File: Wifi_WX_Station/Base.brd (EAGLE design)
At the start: 91.4 x 50.8 mm, 75 parts, among them IC1 3.3v, J1 RJ45-8VERT, J5 RJ11-6RJ11-VERT_LP, J6 M05X22X5FE, Q1 32.768Khz, U1 CP2104-GM, U2 25LC512, U3 PIC24FJ128GA008

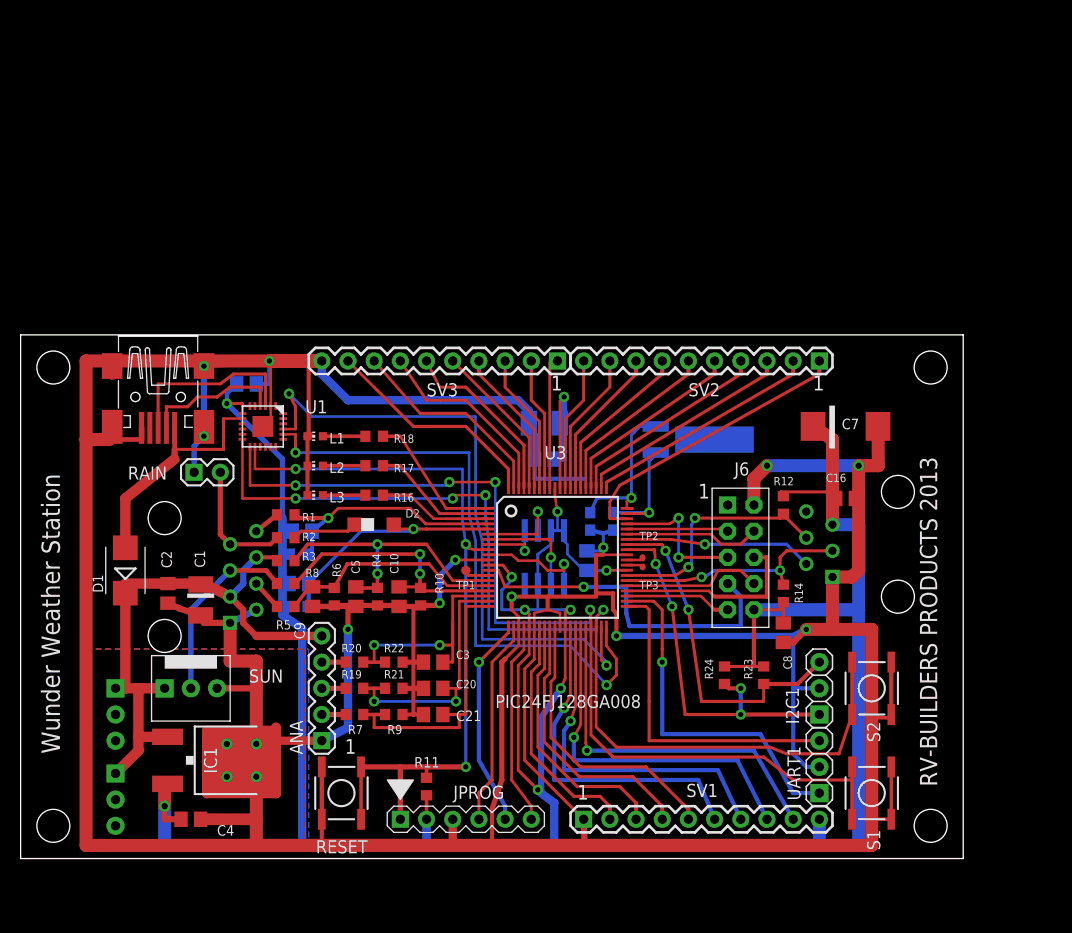
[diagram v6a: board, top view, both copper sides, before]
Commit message: added SILabs Hygrometer board Added frames to the schematics
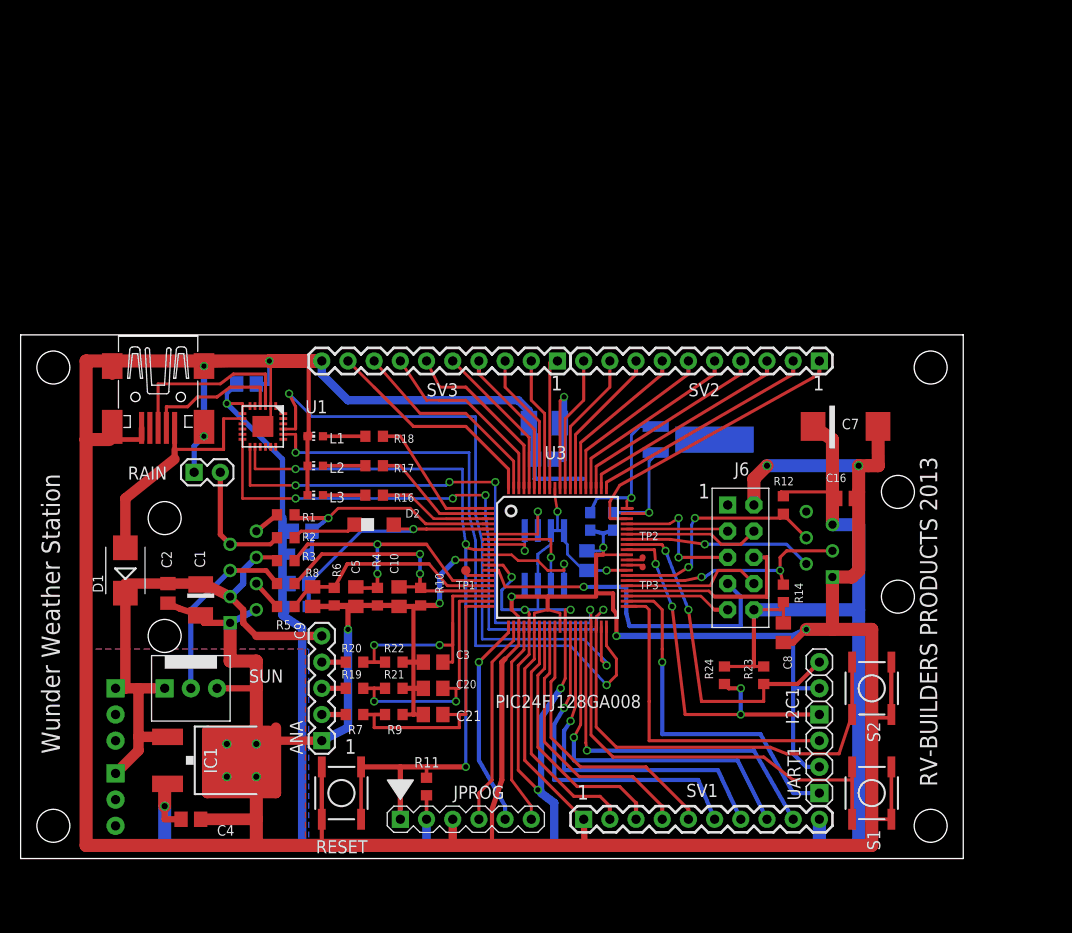
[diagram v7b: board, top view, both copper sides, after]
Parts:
- C7: value 330uF/6V -> 220uF/6.3V
- R19, R20, R7: value 14k -> 100K

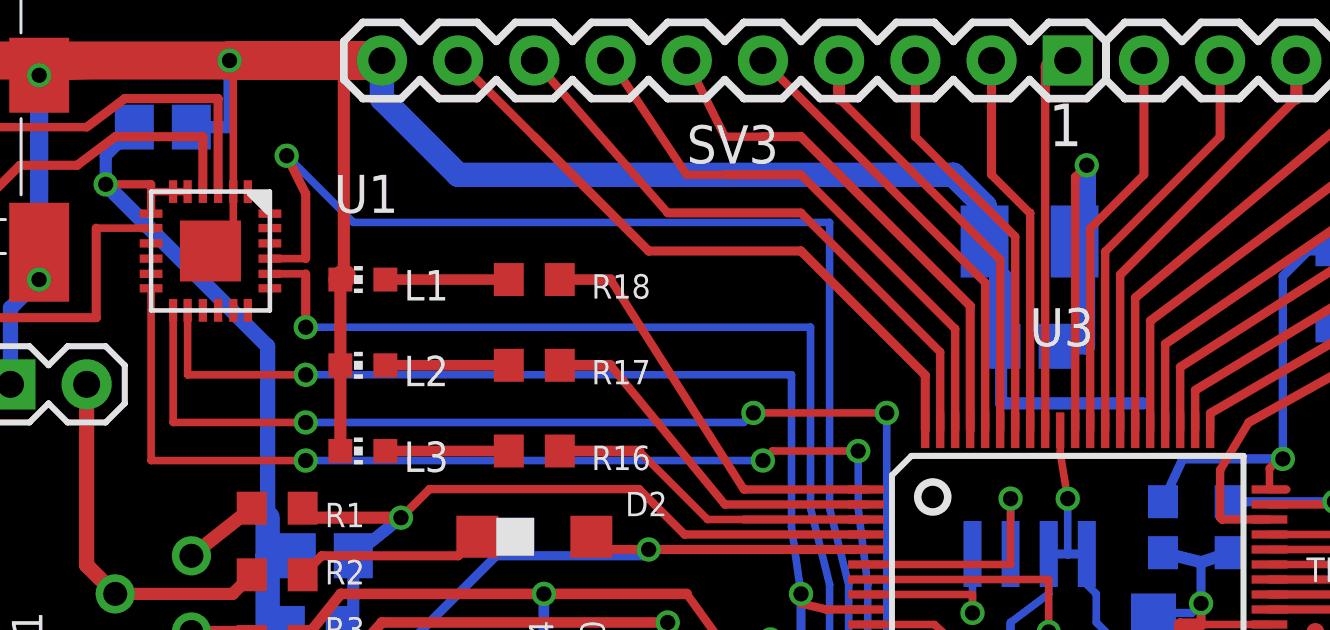
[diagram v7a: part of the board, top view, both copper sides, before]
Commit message: Added multiple new boards - H-pwrdist- Insp_Wind_enc, 5040 etc..
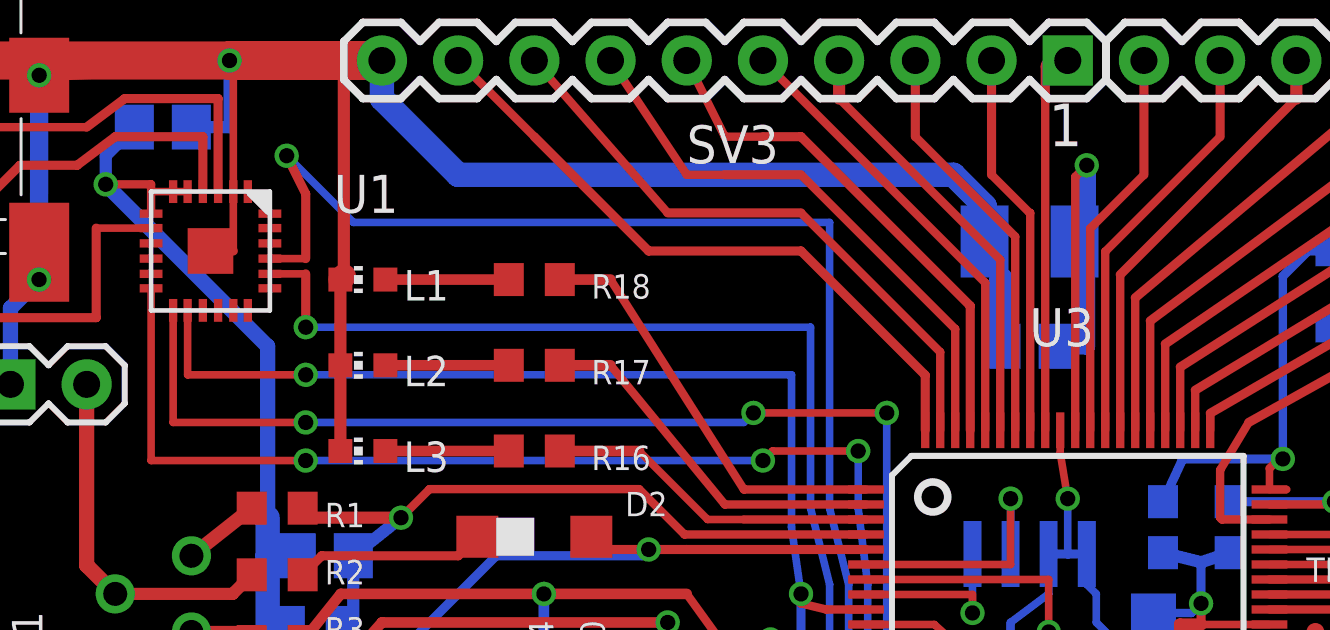
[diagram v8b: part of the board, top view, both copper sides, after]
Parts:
- J5: value RJ11-6RJ11-VERT_LP -> RJ11-6VERT_LP
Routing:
- net GND: track 621.8 -> 615.1 mm
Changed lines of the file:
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@@
 <grid distance="0.05" unitdist="inch" unit="inch" style="lines" multiple="1" display="yes" altdistance="0.0125" altunitdist="inch" altunit="inch"/>
 <layers>
-<layer number="1" name="Top" color="4" fill="1" visible="yes" active="yes"/>
+<layer number="1" name="Top" color="4" fill="1" visible="no" active="yes"/>
 <layer number="16" name="Bottom" color="1" fill="1" visible="yes" active="yes"/>
 <layer number="17" name="Pads" color="2" fill="1" visible="yes" active="yes"/>
@@
 </class>
 </classes>
-<designrules name="Elecrow_2-layer_with reduced cream mask">
+<designrules name="Elecrow_2-layer_with reduced cream mask *">
 <description language="de">&lt;b&gt;EAGLE Design Rules&lt;/b&gt;
 &lt;p&gt;
@@
 <param name="mlMinStopFrame" value="2mil"/>
 <param name="mlMaxStopFrame" value="2mil"/>
-<param name="mlMinCreamFrame" value="2mil"/>
-<param name="mlMaxCreamFrame" value="2mil"/>
+<param name="mlMinCreamFrame" value="1.5mil"/>
+<param name="mlMaxCreamFrame" value="1.5mil"/>
 <param name="mlViaStopLimit" value="100mil"/>
 <param name="srRoundness" value="0"/>
@@
 <attribute name="NAME" x="37.3175" y="33.0675" size="0.8128" layer="25"/>
 </element>
-<element name="J5" library="wifi_WX" package="RJ11-6-VERT" value="RJ11-6RJ11-VERT_LP" x="82.55" y="30.48" rot="MR270"/>
+<element name="J5" library="wifi_WX" package="RJ11-6-VERT" value="RJ11-6VERT_LP" x="82.55" y="30.48" rot="MR270"/>
 </elements>
 <signals>
@@
 <wire x1="76.2" y1="8.89" x2="74.93" y2="10.16" width="0.4064" layer="16"/>
 <wire x1="74.93" y1="10.16" x2="74.93" y2="16.51" width="0.4064" layer="16"/>
-<wire x1="54.61" y1="36.83" x2="49.85" y2="36.83" width="0.4064" layer="16"/>
-<wire x1="49.85" y1="36.83" x2="49.85" y2="38.735" width="0.4064" layer="16"/>
 <wire x1="76.2" y1="22.225" x2="78.74" y2="22.225" width="1.27" layer="1"/>
 <wire x1="78.74" y1="22.225" x2="82.55" y2="22.225" width="1.27" layer="1"/>
